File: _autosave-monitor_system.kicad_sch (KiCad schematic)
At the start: 2 parts, among them K1 DIPxx-1Axx-11x, U1 ACS781xLRTR-050B

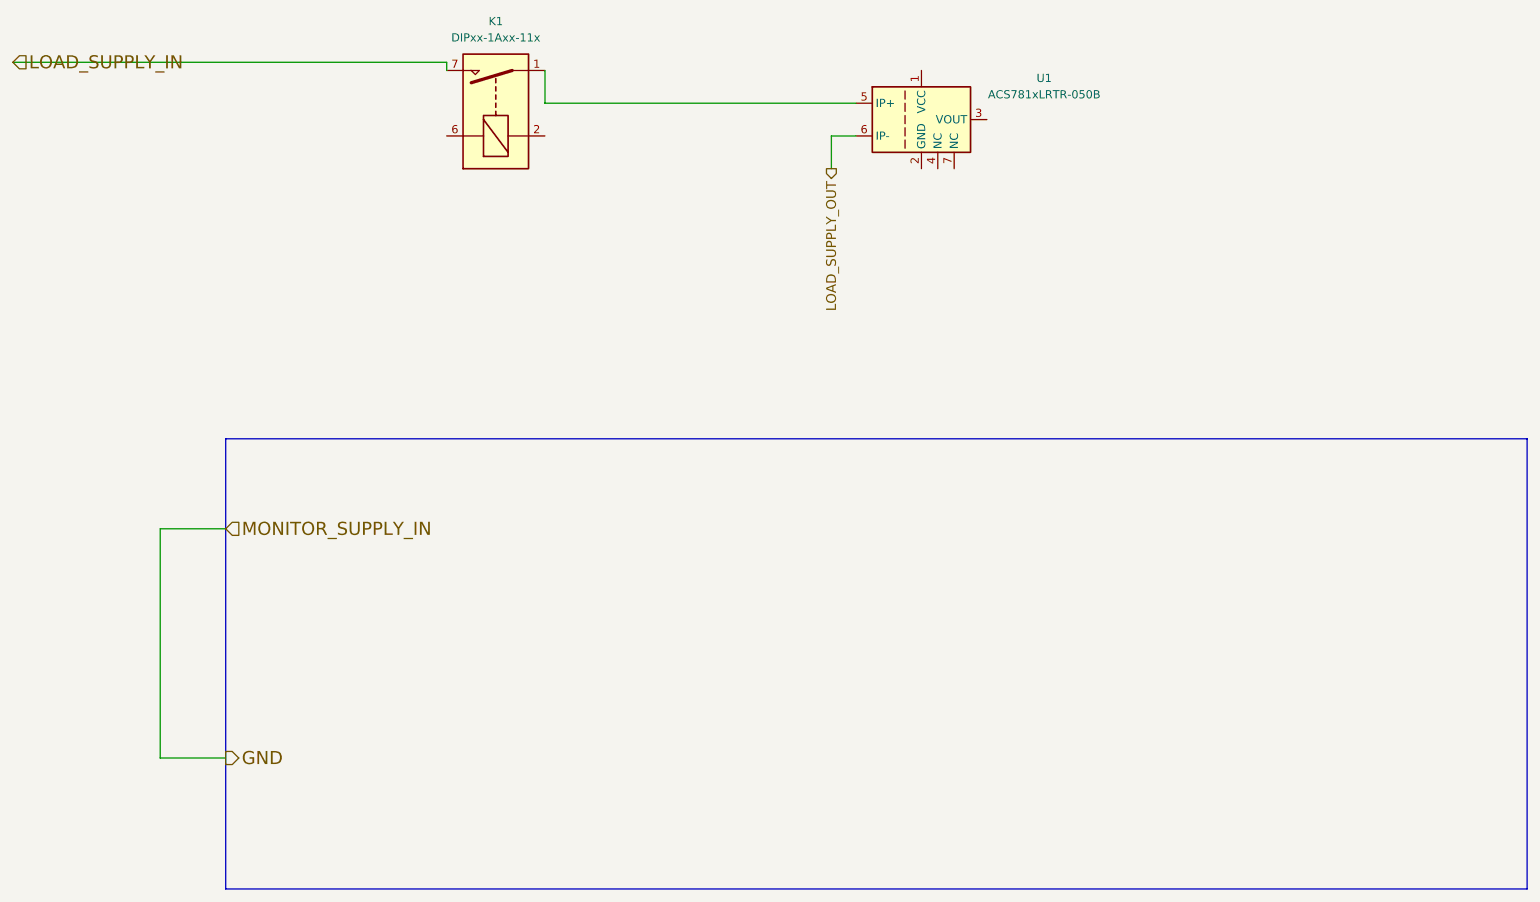
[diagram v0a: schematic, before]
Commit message: feat:added resistor as a load and added demo connections to minimize ERC errors(2)
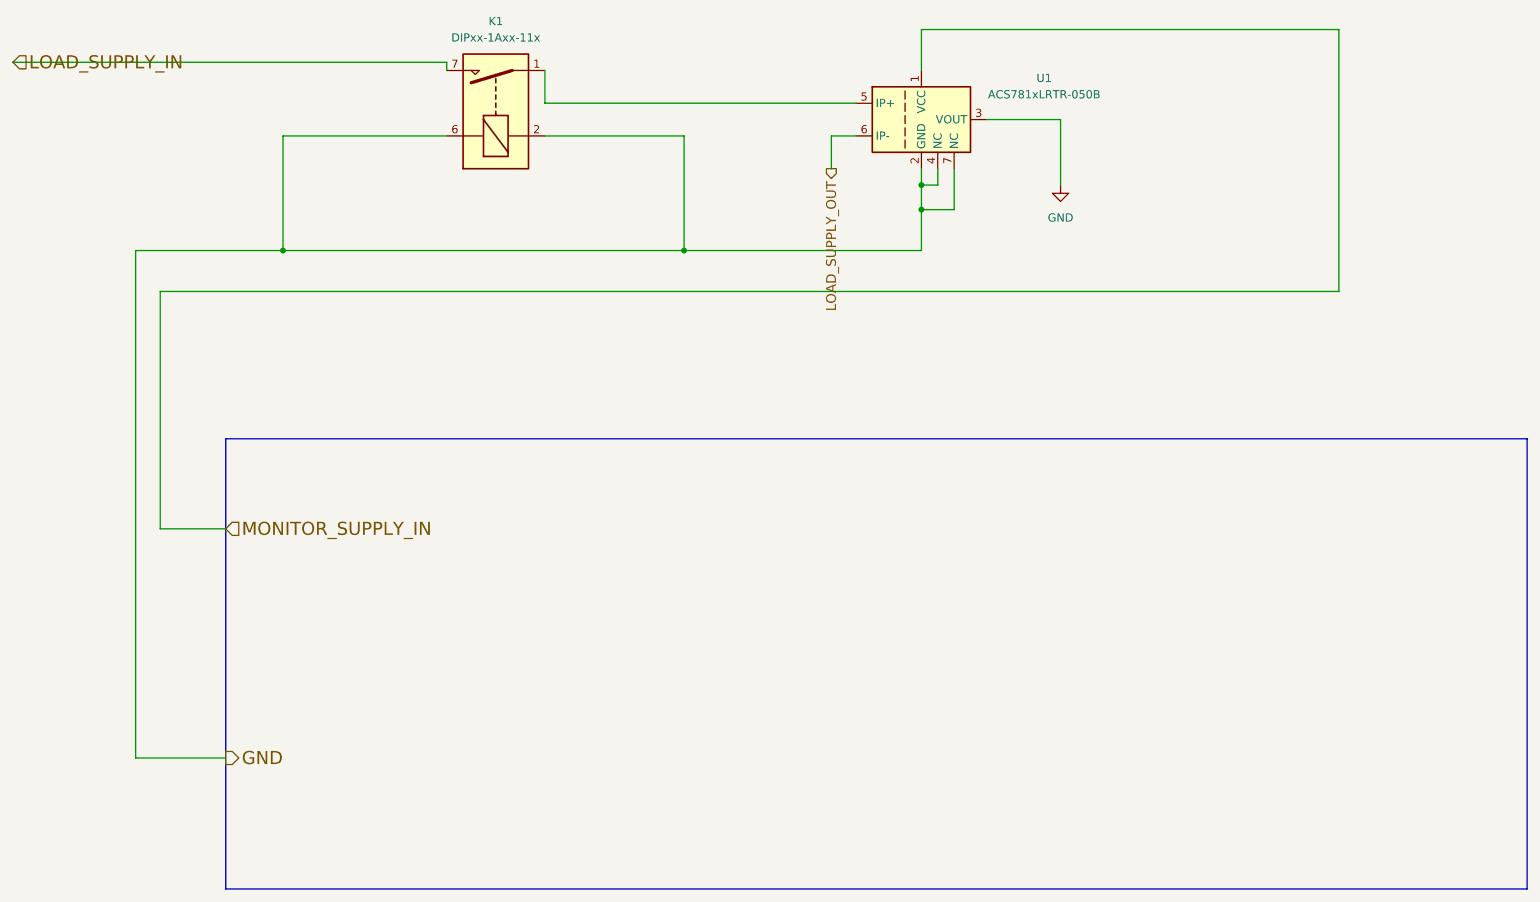
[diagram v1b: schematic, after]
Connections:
- net GND: now also K1.2, K1.6, U1.2 (GND), U1.3 (VOUT), U1.4 (NC), U1.7 (NC)
- net MONITOR_SUPPLY_IN: now reaches U1.1 (VCC)
